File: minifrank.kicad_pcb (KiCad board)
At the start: 2 copper layers, 54 x 58 mm, 76 parts, among them SW1 Reset Button, SW2 Flash Button, U1 W25Q128JVS, U2 NCP1117-3.3_SOT223, U3 RP2040, Y1 ABM8-272-T3

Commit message: HW Rev 1.3
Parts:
- C1, C10, C11, C13, C14, C15, C16, C17, C18, C19, C2, C20, C23, C24, C3, C4, C5, C6, C7, C8, C9: footprint Capacitor_SMD:C_0805_2012Metric_Pad1.18x1.45mm_HandSolder -> LIBS:Medved_C_0805
- C21, C22: footprint LIBS:Medved_CP_Radial_D5.0mm_P2.50mm -> LIBS:Medved_C_0805
- D1, D2, D3: footprint LIBS:R_0805_PLUS -> LIBS:Medved_D_0805
- R1, R10, R11, R12, R13, R14, R15, R16, R17, R18, R19, R2, R20, R21, R22, R23, R24, R25, R26, R27, R28, R29, R30, R31, R32, R4, R5, R6, R7, R8, R9: footprint Resistor_SMD:R_0805_2012Metric_Pad1.20x1.40mm_HandSolder -> LIBS:Medved_R_0805
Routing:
- net /GPIO16: track 37.9 -> 40.0 mm, vias 2 -> 3
- net /R: track 26.0 -> 27.6 mm, vias 0 -> 1
- net /L: track 43.2 -> 44.8 mm, vias 2 -> 3
- net /GPIO0: track 44.3 -> 45.6 mm, vias 3 -> 4
- net Net-(C21-Pad1): track 26.9 -> 28.0 mm, vias 1 -> 2
- net Net-(C22-Pad1): track 50.1 -> 51.2 mm, vias 2 -> 3
- net /GPIO1: track 46.9 -> 47.9 mm, vias 3 -> 4
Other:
- board text added: "HW Rev. 1.3"

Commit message: HW Rev 1.4
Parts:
- added C30: 0.1u, Capacitor_SMD:C_0805_2012Metric_Pad1.18x1.45mm_HandSolder, B.Cu at (103.0, 59.0)
- added D4: 3V3, LIBS:Medved_D_0805, F.Cu at (131.2, 76.2)
- added DB2: Joystick, Connector_Dsub:DSUB-9_Male_EdgeMount_P2.77mm, F.Cu at (116.7, 75.5)
- added JP1: JMP PSRAM, Jumper:SolderJumper-2_P1.3mm_Open_RoundedPad1.0x1.5mm, B.Cu at (117.0, 59.5)
- added PSR1: PSRAM, Package_SO:SO-8_5.3x6.2mm_P1.27mm, B.Cu at (109.4, 59.2)
- added R3: 1k, LIBS:Medved_R_0805, F.Cu at (131.2, 80.0)
- moved AU1 55.4 mm to (130.1, 25.7), turned to 0 degrees
- moved R5 36.3 mm to (93.0, 25.6), turned to 0 degrees
- moved SW2 29.9 mm to (135.7, 40.3), turned to 90 degrees
- moved C19 26.3 mm to (126.2, 67.4)
- moved C4 25.2 mm to (136.8, 53.0), turned to 0 degrees
- moved R1 23.8 mm to (132.0, 43.2), turned to 0 degrees
- moved C6 22.3 mm to (136.8, 49.6), turned to 0 degrees
- moved C24 21.3 mm to (115.2, 66.4)
- moved C21 18.8 mm to (126.2, 70.8)
- moved C23 15.3 mm to (115.2, 63.0)
- moved U2 14.0 mm to (121.3, 30.0)
- moved R2 13.2 mm to (126.2, 64.0), turned to 0 degrees
- moved USB1 12.9 mm to (109.7, 23.1)
- moved SW1 12.6 mm to (135.7, 34.6), turned to 90 degrees
- moved R31 12.0 mm to (110.2, 63.0)
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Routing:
- net /GPIO21: track 0.00 -> 55.9 mm, vias 0 -> 5
- net +3V3: track 232.8 -> 278.4 mm, vias 7 -> 14
- net /R: track 27.6 -> 68.8 mm, vias 1 -> 7
- net /L: track 44.8 -> 85.8 mm, vias 3 -> 6
- net /J1_DATA: track 9.60 -> 48.7 mm
- net /D+: track 7.88 -> 44.3 mm, vias 0 -> 2
- net /GPIO17: track 0.00 -> 36.2 mm, vias 0 -> 4
- net /GPIO20: track 0.00 -> 34.1 mm, vias 0 -> 3
- net Net-(C22-Pad1): track 51.2 -> 17.7 mm, vias 3 -> 0
- net /GPIO15: track 29.8 -> 60.3 mm, vias 4 -> 5
- net /GPIO19: track 0.00 -> 25.8 mm, vias 0 -> 3
- net /GPIO14: track 26.3 -> 49.8 mm, vias 2 -> 8
- net /GPIO18: track 0.00 -> 22.8 mm, vias 0 -> 5
- net /RUN: track 18.1 -> 40.2 mm
- net GND: track 32.9 -> 12.9 mm, vias 61 -> 77
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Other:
- outline, holes or cut-outs redrawn
- board text added: "HW Rev. 1.4"
- board text removed: "HW Rev. 1.2"
- board text removed: "HW Rev. 1.3"

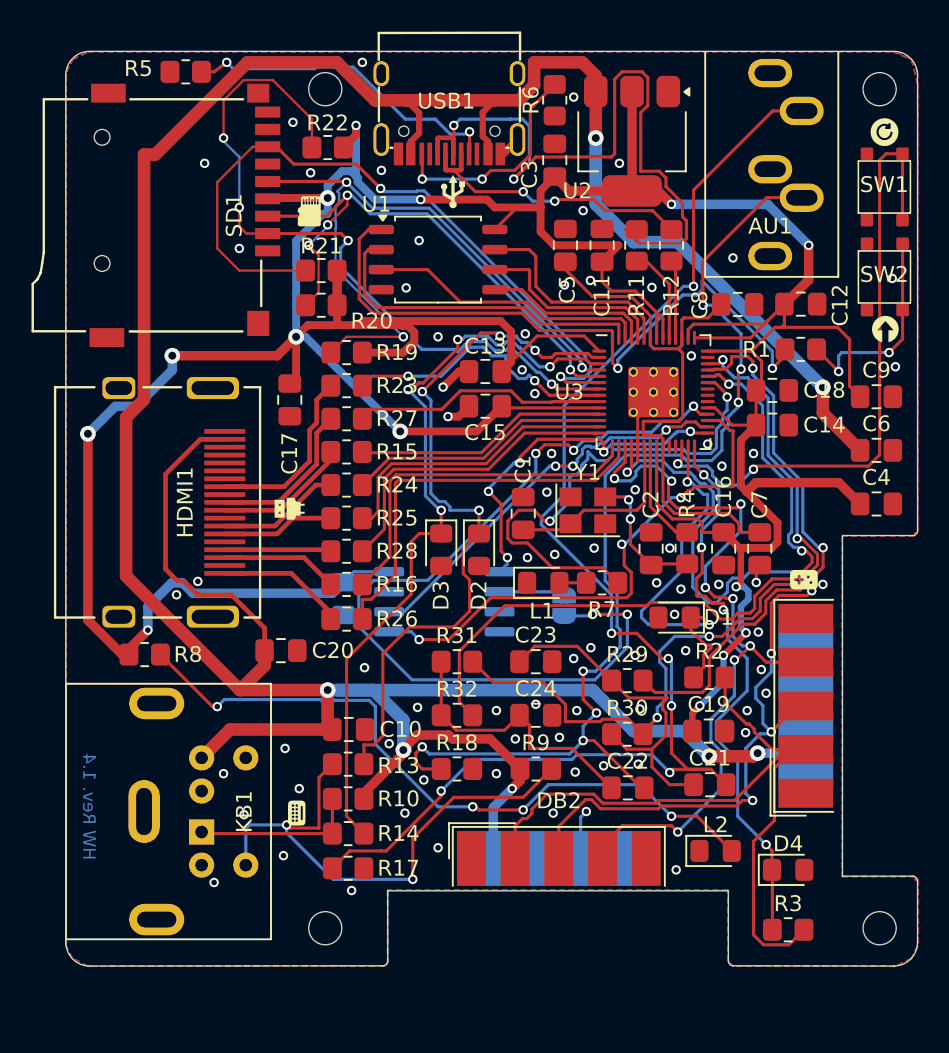
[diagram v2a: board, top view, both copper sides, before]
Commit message: Updates to HW Rev 1.4
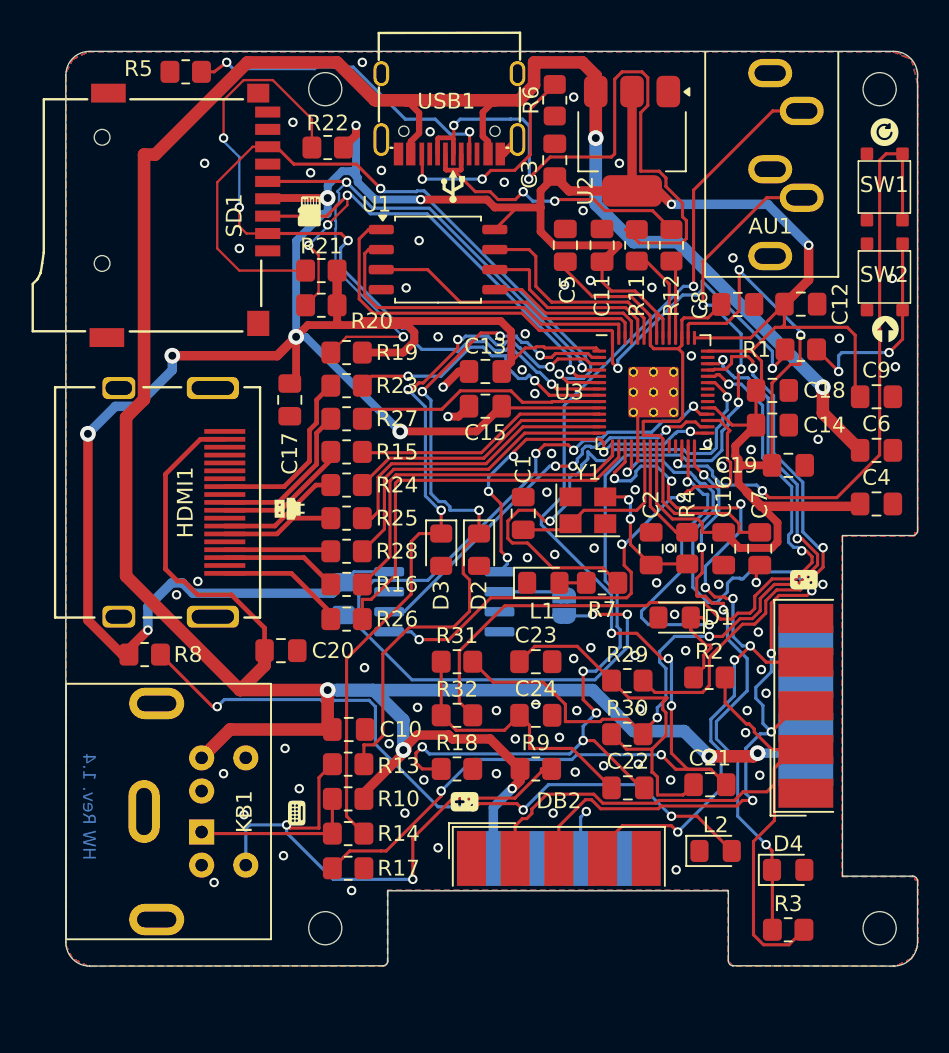
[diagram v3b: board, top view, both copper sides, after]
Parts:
- C12: footprint Capacitor_SMD:C_0805_2012Metric_Pad1.18x1.45mm_HandSolder -> LIBS:Medved_C_0805
- moved C19 17.6 mm to (131.2, 50.5)
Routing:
- net +3V3: track 278.4 -> 282.3 mm, vias 14 -> 12
- net Net-(C21-Pad1): track 22.1 -> 23.5 mm
- net /D+: track 44.3 -> 43.0 mm
- net /RUN: track 40.2 -> 40.9 mm
- net /J1_DATA: track 48.7 -> 49.3 mm
- net GND: vias 77 -> 83

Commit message: HW Rev 1.5
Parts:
- removed C30: 0.1u, Capacitor_SMD:C_0805_2012Metric_Pad1.18x1.45mm_HandSolder
- added C25: 10n, LIBS:Medved_C_0805, F.Cu at (89.0, 83.8)
- added C26: 0.1u, Capacitor_SMD:C_0805_2012Metric_Pad1.18x1.45mm_HandSolder, B.Cu at (102.1, 55.4)
- added JP2: I2S, LIBS:Medved_PinHeader_1x02, F.Cu at (129.2, 83.4)
- added JP3: JMP PSRAM, Jumper:SolderJumper-2_P1.3mm_Open_RoundedPad1.0x1.5mm, B.Cu at (110.2, 51.0)
- added TDA1: TDA1387T, Package_SO:SO-8_5.3x6.2mm_P1.27mm, B.Cu at (119.4, 59.1)
- C10: value 0.1u -> 10u
- C20: value 0.1u -> 10u; footprint LIBS:Medved_C_0805 -> LIBS:Medved_CP_Radial_D5.0mm_P2.50mm
- C21: value 10u -> 0.1u
- C23: value 10n -> 10u
- C5: value 100n -> 0.1u
- C6: value 10u -> 100n
- C7: value 100n -> 10u
- C8: value 1u -> 100n
- C9: value 10u -> 1u
- JP1: value JMP PSRAM -> Audio Jumpers; footprint Jumper:SolderJumper-2_P1.3mm_Open_RoundedPad1.0x1.5mm -> LIBS:Medved_JMP_2x03; moved to F.Cu
- R11, R12: value 27 -> 100R
- R13, R14: value 100R -> 27; moved to B.Cu
- R3: moved to B.Cu
- SW1: value Reset Button -> Flash Button
- SW2: value Flash Button -> Reset Button
- moved R14 49.7 mm to (122.4, 28.0), turned to -90 degrees
- moved R3 47.3 mm to (136.7, 33.0), turned to 90 degrees
- moved R13 44.8 mm to (120.2, 28.0), turned to -90 degrees
- moved D4 38.9 mm to (107.8, 45.1), turned to -90 degrees
- moved R8 25.7 mm to (113.9, 72.9)
- moved JP1 24.6 mm to (129.2, 80.8), turned to 90 degrees
- moved C20 22.4 mm to (119.3, 71.9)
- moved C22 11.1 mm to (131.3, 75.2)
- moved C21 3.90 mm to (126.2, 66.9), turned to 90 degrees
- moved DB2 3.50 mm to (116.7, 79.0)
- moved REF** 3.49 mm to (137.0, 83.4)
- moved REF** 3.49 mm to (101.8, 83.4)
- moved R2 0.10 mm to (126.2, 63.9)
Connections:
- AU1 pad R: /R -> Net-(AU1-PadR)
- AU1 pad T: /L -> Net-(AU1-PadT)
- C10 pad 1: VBUS -> +3V3
- C20 pad 1: VBUS -> /FLT
- C21 pad 1: Net-(C21-Pad1) -> VBUS
- C21 pad 2: /L -> GND
- C22 pad 2: /R -> Net-(AU1-PadT)
- C23 pad 1: Net-(C21-Pad1) -> Net-(C23-Pad1)
- C23 pad 2: GND -> Net-(AU1-PadR)
- C5 pad 1: +1V1 -> VBUS
- C6 pad 1: VBUS -> +1V1
- C7 pad 1: +1V1 -> VBUS
- C9 pad 1: +3V3 -> +1V1
- D2 pad 1: /GPIO0 -> /GPIO17
- D3 pad 1: /GPIO1 -> /GPIO0
- D4 pad 1: /GPIO17 -> /GPIO1
- JP1 pad 1: Net-(JP1-A) -> /RIGHT_OUT
- JP1 pad 2: /GPIO21 -> /GPIO26
- PSR1 pad 2: Net-(JP1-A) -> Net-(JP3-A)
- R1 pad 1: /QSPI_SS -> /GPIO16
- R1 pad 2: /~{USB_BOOT} -> /J1_DATA
- R11 pad 1: /D+ -> /PS/2 CLK
- R11 pad 2: Net-(U3-USB_DP) -> /GPIO0
- R12 pad 1: /D- -> /PS/2 DATA
- R12 pad 2: Net-(U3-USB_DM) -> /GPIO1
- R13 pad 1: /PS/2 CLK -> /D+
- R13 pad 2: /GPIO0 -> Net-(U3-USB_DP)
- R14 pad 1: /PS/2 DATA -> /D-
- R14 pad 2: /GPIO1 -> Net-(U3-USB_DM)
- R17 pad 1: /L -> Net-(AU1-PadT)
- R18 pad 1: /R -> Net-(AU1-PadR)
- R2 pad 1: /GPIO16 -> /GPIO17
- R29 pad 1: Net-(C21-Pad1) -> Net-(C22-Pad1)
- R29 pad 2: /GPIO27 -> /LEFT_OUT
- R3 pad 1: /GPIO17 -> /QSPI_SS
- R3 pad 2: /J1_DATA -> /~{USB_BOOT}
- R30 pad 1: Net-(C21-Pad1) -> Net-(C22-Pad1)
- R30 pad 2: /GPIO28 -> /BEEP_OUT
- R31 pad 1: Net-(C22-Pad1) -> Net-(C23-Pad1)
- R31 pad 2: /GPIO28 -> /BEEP_OUT
- R32 pad 1: Net-(C22-Pad1) -> Net-(C23-Pad1)
- R32 pad 2: /GPIO26 -> /RIGHT_OUT
- SW1 pad 3: /RUN -> /~{USB_BOOT}
- SW1 pad 4: /RUN -> /~{USB_BOOT}
- SW2 pad 3: /~{USB_BOOT} -> /RUN
- SW2 pad 4: /~{USB_BOOT} -> /RUN
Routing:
- net GND: track 12.9 -> 204.1 mm, vias 83 -> 110
- net Net-(AU1-PadT): track 0.00 -> 103.7 mm, vias 0 -> 6
- net /L: track 85.6 -> 0.00 mm, vias 6 -> 0
- net /PS/2 CLK: track 34.6 -> 113.7 mm, vias 2 -> 6
- net /PS/2 DATA: track 10.5 -> 83.2 mm, vias 0 -> 6
- net Net-(AU1-PadR): track 0.00 -> 70.3 mm, vias 0 -> 6
- net /R: track 68.8 -> 0.00 mm, vias 7 -> 0
- net /RIGHT_TDA: track 0.00 -> 64.7 mm, vias 0 -> 6
- net /BEEP_OUT: track 0.00 -> 55.5 mm, vias 0 -> 2
- net /LEFT_TDA: track 0.00 -> 54.7 mm, vias 0 -> 7
- net /GPIO27: track 35.2 -> 76.6 mm, vias 2 -> 6
- net /LEFT_OUT: track 0.00 -> 40.7 mm, vias 0 -> 2
- net /GPIO28: track 49.5 -> 90.1 mm, vias 4 -> 3
- net Net-(C23-Pad1): track 0.00 -> 38.4 mm
- net /RIGHT_OUT: track 0.00 -> 36.7 mm, vias 0 -> 5
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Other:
- board size 54 x 58 mm -> 54 x 61.5 mm
- board text added: "HW Rev. 1.5"
- board text added: "rh1.dev"
- board text removed: "HW Rev. 1.4"
- board text removed: "© 2024 Mikhail Matveev https://rh1.dev"
